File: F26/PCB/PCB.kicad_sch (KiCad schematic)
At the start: 9 parts, among them J1 B3B-XH-A, J2 Raspberry_Pi_4, J3 B2B-XH-A, J4 B3B-XH-A, SW1 SW_Nidec_CAS-120A1, U4 815

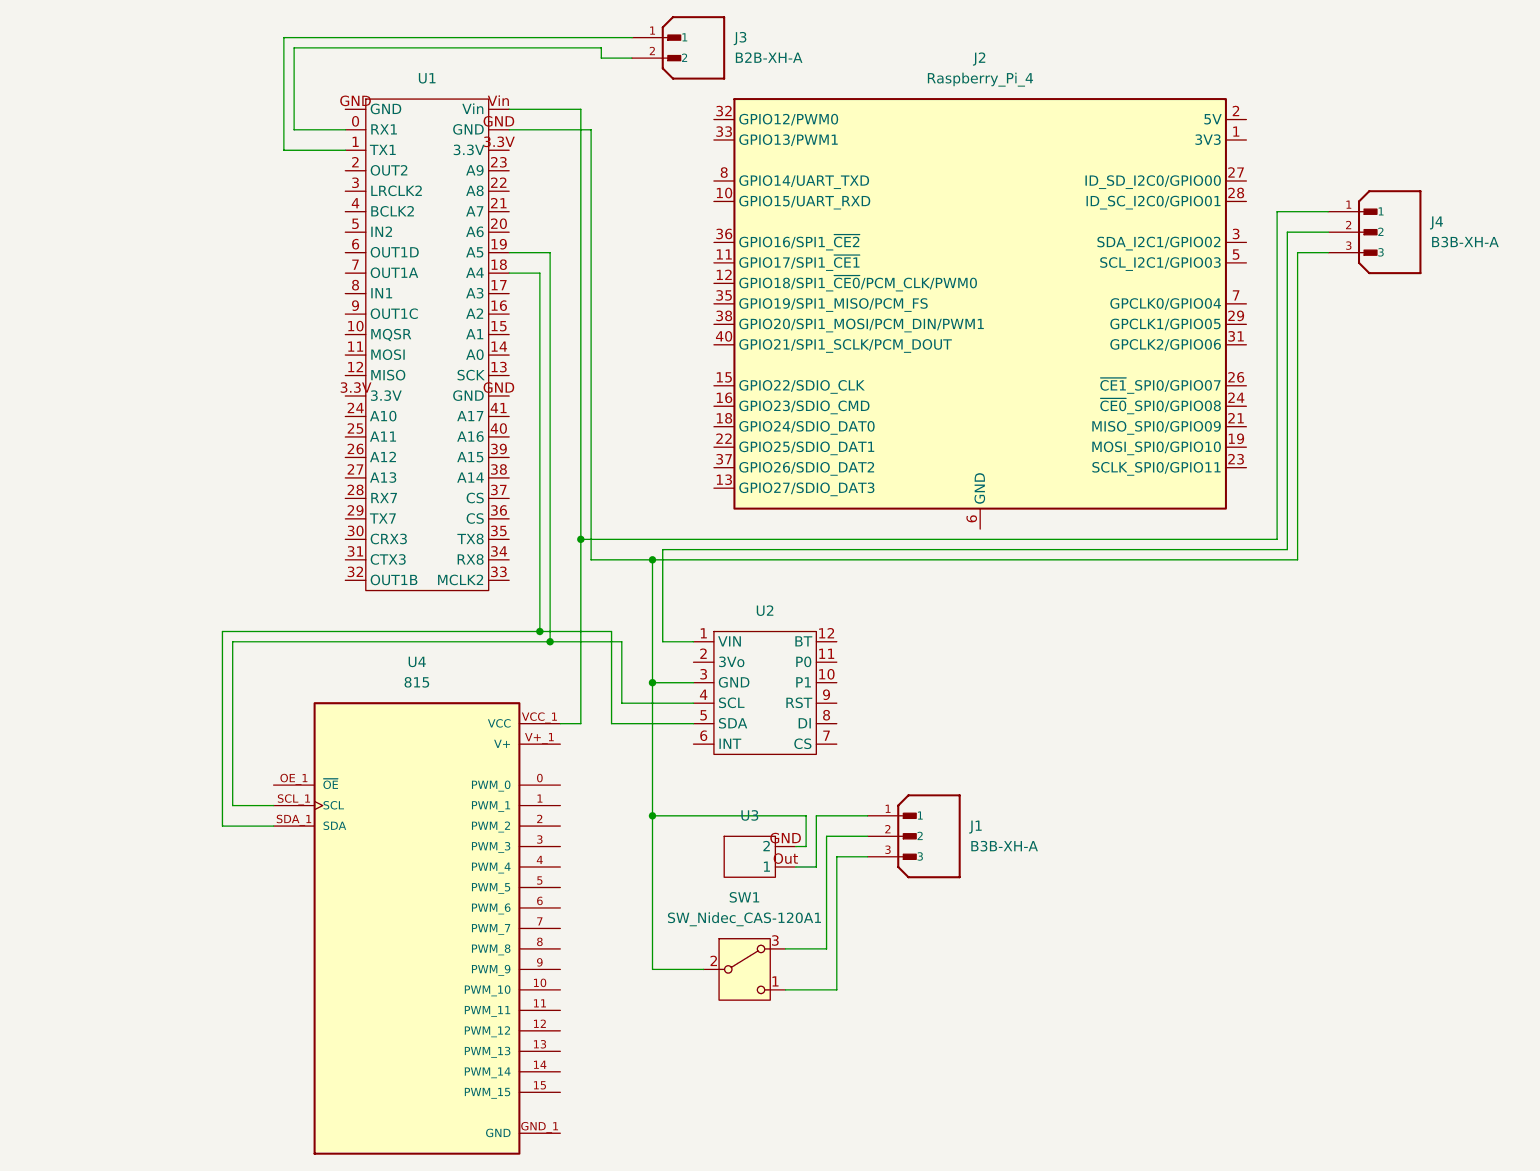
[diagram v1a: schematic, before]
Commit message: Worded on PCB and teensy implementation
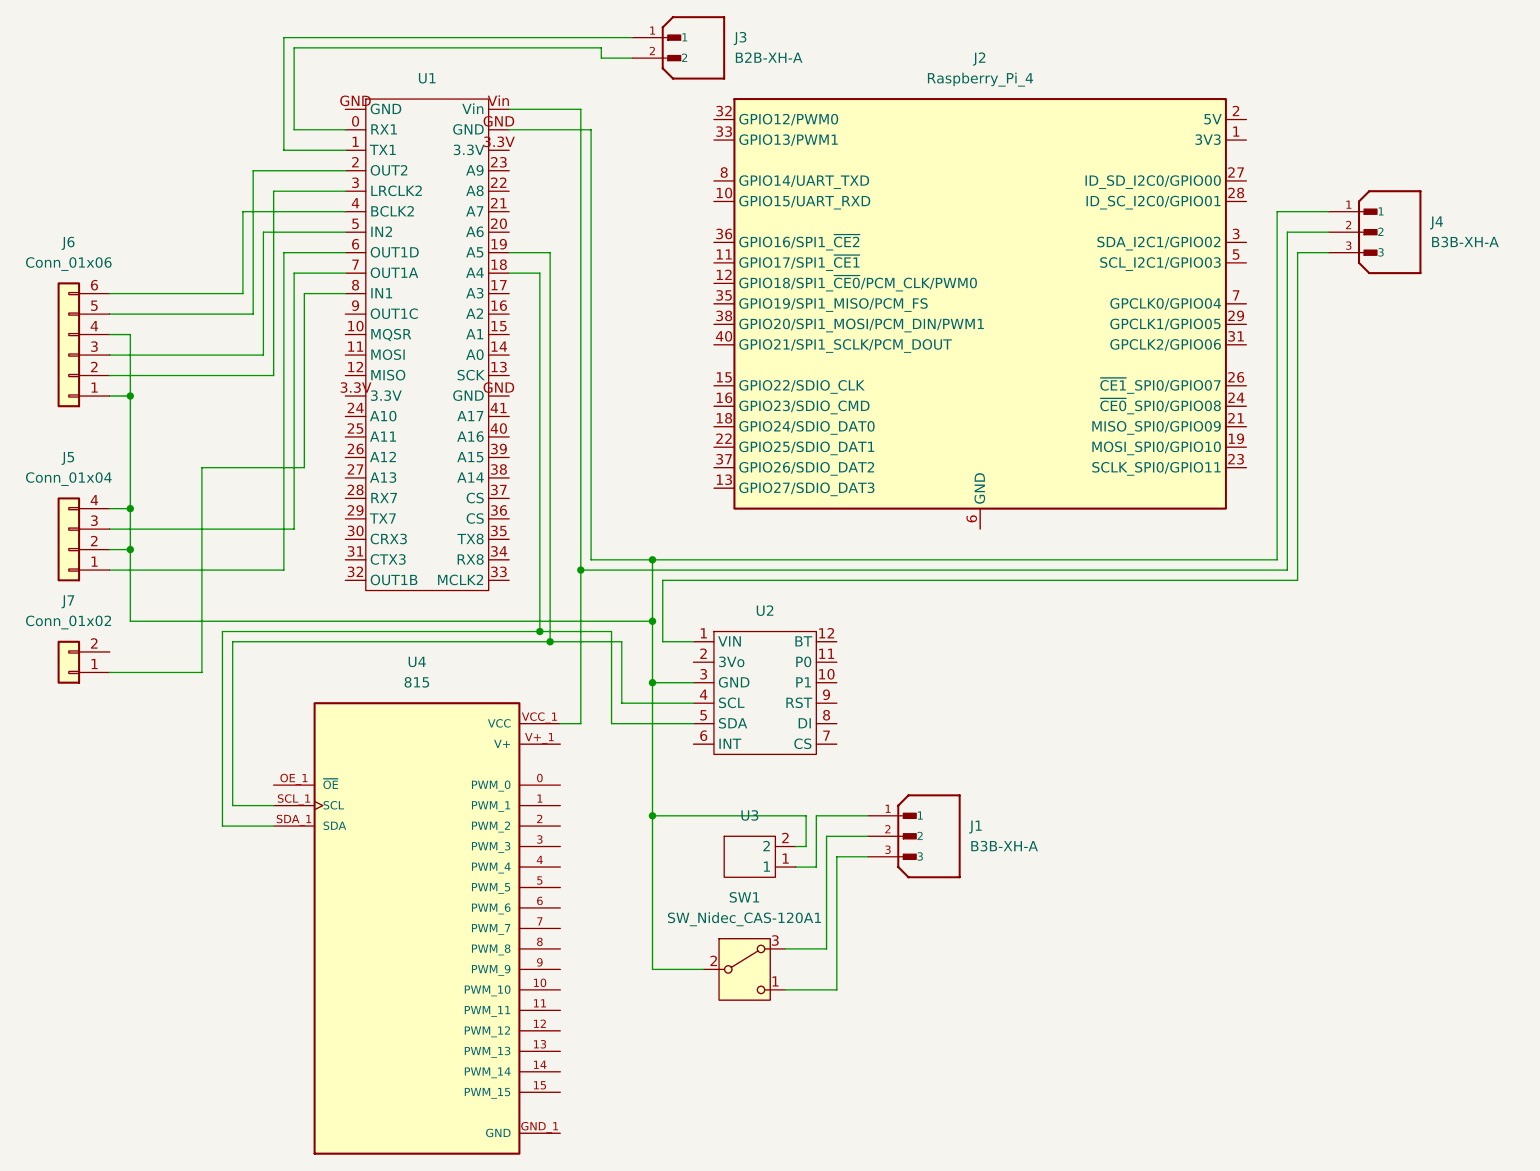
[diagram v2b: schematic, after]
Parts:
- added J5: Conn_01x04, Connector_JST:JST_EH_B4B-EH-A_1x04_P2.50mm_Vertical, symbol Connector_Generic:Conn_01x04
- added J6: Conn_01x06, Connector_JST:JST_EH_B6B-EH-A_1x06_P2.50mm_Vertical, symbol Connector_Generic:Conn_01x06
- added J7: Conn_01x02, Connector_JST:JST_EH_B2B-EH-A_1x02_P2.50mm_Vertical, symbol Connector_Generic:Conn_01x02
- J1: footprint B3B-XH-A:JST_B3B-XH-A -> Connector_JST:JST_EH_B3B-EH-A_1x03_P2.50mm_Vertical
- J3: footprint JST:JST -> Connector_JST:JST_EH_B2B-EH-A_1x02_P2.50mm_Vertical
- J4: footprint JST3:JST3 -> Connector_JST:JST_EH_B3B-EH-A_1x03_P2.50mm_Vertical
- SW1: footprint Button_Switch_SMD:Nidec_Copal_CAS-120A -> Switch:Mini_Toggle_DPDT_4.3x4.6mm
- U3: footprint (none) -> Button:Switch_2Pin_5mm_ParallelBlades
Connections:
- net VCC: now also J4.2; no longer J4.1
- net at U2.1 (VIN): now also J4.3; no longer J4.2
- net at U1.2 (OUT2): now also J6.5 (Pin_5)
- net at U1.3 (LRCLK2): now also J6.2 (Pin_2)
- net at U1.4 (BCLK2): now also J6.6 (Pin_6)
- net at U1.5 (IN2): now also J6.3 (Pin_3)
- net at U1.6 (OUT1D): now also J5.1 (Pin_1)
- net at U1.7 (OUT1A): now also J5.3 (Pin_3)
- net at U1.8 (IN1): now also J7.1 (Pin_1)
- net at J1.1: now also U3.1; no longer U3.Out (1)
- new net: J4.1, J5.2 (Pin_2), J5.4 (Pin_4), J6.1 (Pin_1), J6.4 (Pin_4), SW1.2 (B), U1.GND, U2.3 (GND), U3.2
- now unconnected: U1.GND
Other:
- moved on the sheet: U3
